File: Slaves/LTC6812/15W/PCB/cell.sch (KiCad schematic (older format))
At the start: 6 parts, among them Q2 TSM2323

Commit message: Datasheet update for V1.0
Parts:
- C11: MPN (none) -> GRM188R72A104KA35D
- D5: MPN (none) -> PDZ7.5B
- R13: value 15 -> 22
- R14: value R -> 3.3k
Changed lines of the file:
@@
 F 2 "Capacitors_SMD:C_0603_HandSoldering" H 5688 3650 50  0001 C CNN
 F 3 "~" H 5650 3800 50  0001 C CNN
-F 4 "100V" H 5450 3950 50  0000 C CNN "Voltage"
+F 4 "GRM188R72A104KA35D" H 5650 3800 50  0001 C CNN "MPN"
+F 5 "100V" H 5450 3950 50  0000 C CNN "Voltage"
 	1    5650 3800
 	-1   0    0    1
@@
 AR Path="/5B5115CC/5C6D9E32" Ref="R81"  Part="1"
 F 0 "R69" V 3193 4650 50  0000 C CNN
-F 1 "15" V 3284 4650 50  0000 C CNN
+F 1 "22" V 3284 4650 50  0000 C CNN
 F 2 "Resistors_SMD:R_2512" V 3330 4650 50  0001 C CNN
 F 3 "~" H 3400 4650 50  0001 C CNN
+F 4 "" V 3400 4650 50  0001 C CNN "MPN"
 	1    3400 4650
 	-1   0    0    1
@@
 F 2 "TO_SOT_Packages_SMD:SOT-23" H 3700 4200 50  0001 C CNN
 F 3 "~" H 3500 4100 50  0001 C CNN
+F 4 "" H 3500 4100 50  0001 C CNN "MPN"
 	1    3500 4100
 	-1   0    0    1
@@
 F 2 "Diode_SMD:D_SOD-323_HandSoldering" H 6900 3950 50  0001 C CNN
 F 3 "~" H 6900 3950 50  0001 C CNN
+F 4 "PDZ7.5B" V 6900 3950 50  0001 C CNN "MPN"
 	1    6900 3950
 	0    1    1    0
@@
 F 2 "Resistors_SMD:R_0603_HandSoldering" V 4980 3250 50  0001 C CNN
 F 3 "~" H 5050 3250 50  0001 C CNN
+F 4 "" V 5050 3250 50  0001 C CNN "MPN"
 	1    5050 3250
 	0    1    1    0
@@
 AR Path="/5B5115CC/5B4FCD21" Ref="R82"  Part="1"
 F 0 "R70" V 4593 4100 50  0000 C CNN
-F 1 "R" V 4684 4100 50  0000 C CNN
+F 1 "3.3k" V 4684 4100 50  0000 C CNN
 F 2 "Resistors_SMD:R_0603_HandSoldering" V 4730 4100 50  0001 C CNN
 F 3 "~" H 4800 4100 50  0001 C CNN
+F 4 "" V 4800 4100 50  0001 C CNN "MPN"
 	1    4800 4100
 	0    1    1    0

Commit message: maintenance update
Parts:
- C11: footprint Capacitors_SMD:C_0603_HandSoldering -> Capacitor_SMD:C_0603_1608Metric
- D5: footprint Diode_SMD:D_SOD-323_HandSoldering -> Diode_SMD:D_SOD-323
- R13: footprint Resistors_SMD:R_2512 -> Resistor_SMD:R_2512_6332Metric
- R14, R15: footprint Resistors_SMD:R_0603_HandSoldering -> Resistor_SMD:R_0603_1608Metric
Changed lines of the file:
@@
 $Descr A4 11693 8268
 encoding utf-8
-Sheet 16 16
+Sheet 12 16
 Title ""
 Date ""
@@
 AR Path="/5B510167/5B4FCD15" Ref="C27"  Part="1"
 AR Path="/5B5115CC/5B4FCD15" Ref="C28"  Part="1"
-F 0 "C25" H 5535 3754 50  0000 R CNN
+F 0 "C21" H 5535 3754 50  0000 R CNN
 F 1 "100n" H 5535 3845 50  0000 R CNN
-F 2 "Capacitors_SMD:C_0603_HandSoldering" H 5688 3650 50  0001 C CNN
+F 2 "Capacitor_SMD:C_0603_1608Metric" H 5688 3650 50  0001 C CNN
 F 3 "~" H 5650 3800 50  0001 C CNN
 F 4 "GRM188R72A104KA35D" H 5650 3800 50  0001 C CNN "MPN"
@@
 AR Path="/5B510167/5C6D9E32" Ref="R77"  Part="1"
 AR Path="/5B5115CC/5C6D9E32" Ref="R81"  Part="1"
-F 0 "R69" V 3193 4650 50  0000 C CNN
+F 0 "R53" V 3193 4650 50  0000 C CNN
 F 1 "22" V 3284 4650 50  0000 C CNN
-F 2 "Resistors_SMD:R_2512" V 3330 4650 50  0001 C CNN
+F 2 "Resistor_SMD:R_2512_6332Metric" V 3330 4650 50  0001 C CNN
 F 3 "~" H 3400 4650 50  0001 C CNN
 F 4 "" V 3400 4650 50  0001 C CNN "MPN"
@@
 AR Path="/5B510167/5C51375B" Ref="Q18"  Part="1"
 AR Path="/5B5115CC/5C51375B" Ref="Q19"  Part="1"
-F 0 "Q16" H 3705 4054 50  0000 L CNN
+F 0 "Q12" H 3705 4054 50  0000 L CNN
 F 1 "TSM2323" H 3705 4145 50  0000 L CNN
 F 2 "TO_SOT_Packages_SMD:SOT-23" H 3700 4200 50  0001 C CNN
@@
 AR Path="/5B510167/5D68CA39" Ref="D21"  Part="1"
 AR Path="/5B5115CC/5D68CA39" Ref="D22"  Part="1"
-F 0 "D19" V 6854 4029 50  0000 L CNN
+F 0 "D15" V 6854 4029 50  0000 L CNN
 F 1 "PDZ7.5B" V 6945 4029 50  0000 L CNN
-F 2 "Diode_SMD:D_SOD-323_HandSoldering" H 6900 3950 50  0001 C CNN
+F 2 "Diode_SMD:D_SOD-323" H 6900 3950 50  0001 C CNN
 F 3 "~" H 6900 3950 50  0001 C CNN
 F 4 "PDZ7.5B" V 6900 3950 50  0001 C CNN "MPN"
@@
 AR Path="/5B510167/5B4FCD0D" Ref="R79"  Part="1"
 AR Path="/5B5115CC/5B4FCD0D" Ref="R83"  Part="1"
-F 0 "R71" V 4843 3250 50  0000 C CNN
+F 0 "R55" V 4843 3250 50  0000 C CNN
 F 1 "100" V 4934 3250 50  0000 C CNN
-F 2 "Resistors_SMD:R_0603_HandSoldering" V 4980 3250 50  0001 C CNN
+F 2 "Resistor_SMD:R_0603_1608Metric" V 4980 3250 50  0001 C CNN
 F 3 "~" H 5050 3250 50  0001 C CNN
 F 4 "" V 5050 3250 50  0001 C CNN "MPN"
@@
 AR Path="/5B510167/5B4FCD21" Ref="R78"  Part="1"
 AR Path="/5B5115CC/5B4FCD21" Ref="R82"  Part="1"
-F 0 "R70" V 4593 4100 50  0000 C CNN
+F 0 "R54" V 4593 4100 50  0000 C CNN
 F 1 "3.3k" V 4684 4100 50  0000 C CNN
-F 2 "Resistors_SMD:R_0603_HandSoldering" V 4730 4100 50  0001 C CNN
+F 2 "Resistor_SMD:R_0603_1608Metric" V 4730 4100 50  0001 C CNN
 F 3 "~" H 4800 4100 50  0001 C CNN
 F 4 "" V 4800 4100 50  0001 C CNN "MPN"

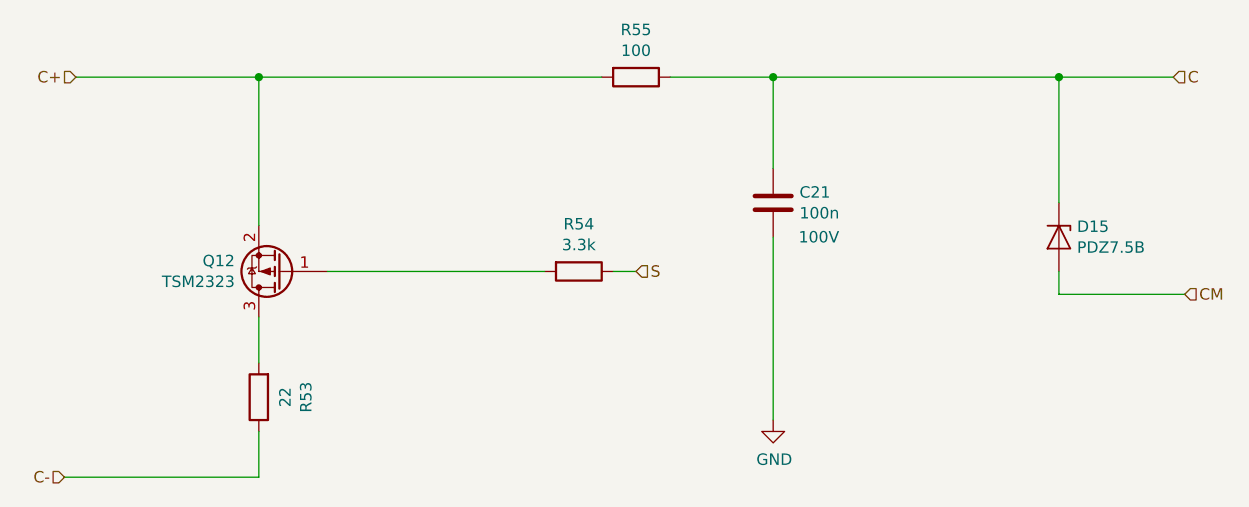
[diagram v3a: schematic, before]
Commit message: Small changes to resistor & connectors
Now with vertical USB connectors & clip connectors
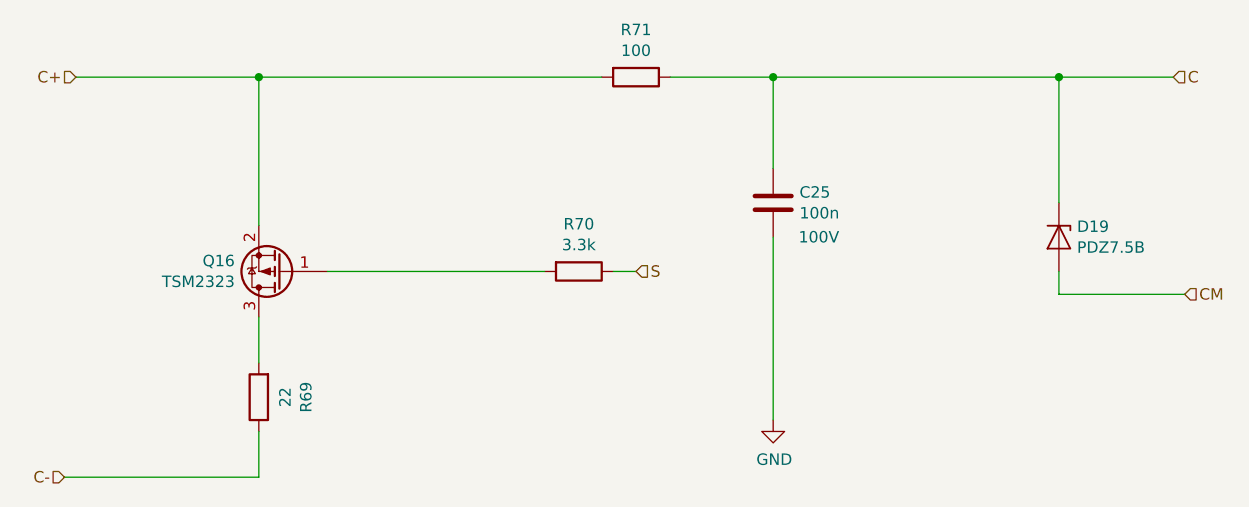
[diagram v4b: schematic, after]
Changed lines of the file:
@@
 AR Path="/5B510167/5B4FCD15" Ref="C27"  Part="1"
 AR Path="/5B5115CC/5B4FCD15" Ref="C28"  Part="1"
-F 0 "C21" H 5535 3754 50  0000 R CNN
+F 0 "C25" H 5535 3754 50  0000 R CNN
 F 1 "100n" H 5535 3845 50  0000 R CNN
 F 2 "Capacitor_SMD:C_0603_1608Metric" H 5688 3650 50  0001 C CNN
@@
 AR Path="/5B510167/5C6D9E32" Ref="R77"  Part="1"
 AR Path="/5B5115CC/5C6D9E32" Ref="R81"  Part="1"
-F 0 "R53" V 3193 4650 50  0000 C CNN
+F 0 "R69" V 3193 4650 50  0000 C CNN
 F 1 "22" V 3284 4650 50  0000 C CNN
 F 2 "Resistor_SMD:R_2512_6332Metric" V 3330 4650 50  0001 C CNN
@@
 AR Path="/5B510167/5C51375B" Ref="Q18"  Part="1"
 AR Path="/5B5115CC/5C51375B" Ref="Q19"  Part="1"
-F 0 "Q12" H 3705 4054 50  0000 L CNN
+F 0 "Q16" H 3705 4054 50  0000 L CNN
 F 1 "TSM2323" H 3705 4145 50  0000 L CNN
 F 2 "TO_SOT_Packages_SMD:SOT-23" H 3700 4200 50  0001 C CNN
@@
 AR Path="/5B510167/5D68CA39" Ref="D21"  Part="1"
 AR Path="/5B5115CC/5D68CA39" Ref="D22"  Part="1"
-F 0 "D15" V 6854 4029 50  0000 L CNN
+F 0 "D19" V 6854 4029 50  0000 L CNN
 F 1 "PDZ7.5B" V 6945 4029 50  0000 L CNN
 F 2 "Diode_SMD:D_SOD-323" H 6900 3950 50  0001 C CNN
@@
 AR Path="/5B510167/5B4FCD0D" Ref="R79"  Part="1"
 AR Path="/5B5115CC/5B4FCD0D" Ref="R83"  Part="1"
-F 0 "R55" V 4843 3250 50  0000 C CNN
+F 0 "R71" V 4843 3250 50  0000 C CNN
 F 1 "100" V 4934 3250 50  0000 C CNN
 F 2 "Resistor_SMD:R_0603_1608Metric" V 4980 3250 50  0001 C CNN
@@
 AR Path="/5B510167/5B4FCD21" Ref="R78"  Part="1"
 AR Path="/5B5115CC/5B4FCD21" Ref="R82"  Part="1"
-F 0 "R54" V 4593 4100 50  0000 C CNN
+F 0 "R70" V 4593 4100 50  0000 C CNN
 F 1 "3.3k" V 4684 4100 50  0000 C CNN
 F 2 "Resistor_SMD:R_0603_1608Metric" V 4730 4100 50  0001 C CNN
